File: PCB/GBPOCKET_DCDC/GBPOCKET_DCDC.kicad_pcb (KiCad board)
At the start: 2 copper layers, 23 parts, among them J1 Conn_01x03, J2 Conn_01x02, U1 MCP1623, U2 MAX868

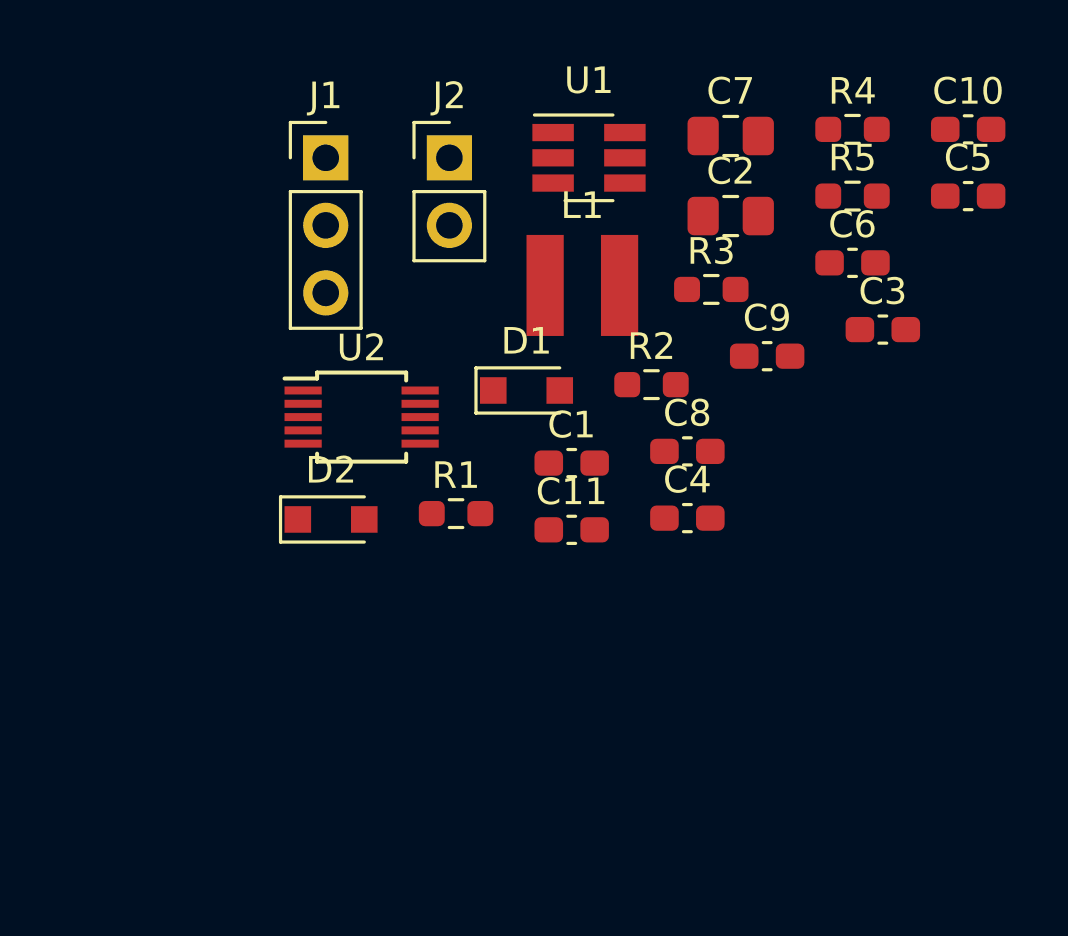
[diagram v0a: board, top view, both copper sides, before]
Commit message: Updated schematic a bit Added header for LED Finished PCB (quick'n'dirty, bit it'll do) Exported gerbers for production
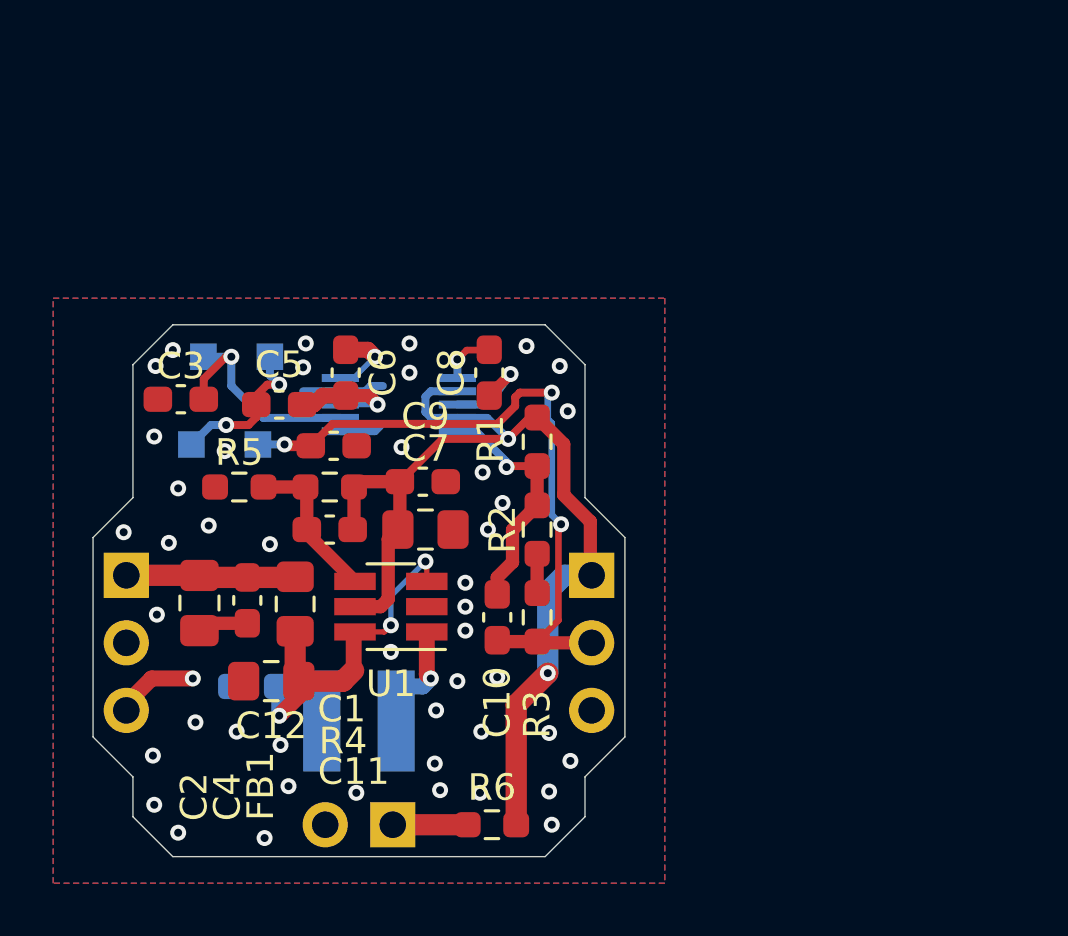
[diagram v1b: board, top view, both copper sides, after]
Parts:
- added C12: 10uF, Capacitor_SMD:C_0805_2012Metric_Pad1.18x1.45mm_HandSolder, F.Cu at (125.2, 93.4)
- added C13: 100nF, Capacitor_SMD:C_0603_1608Metric_Pad1.08x0.95mm_HandSolder, B.Cu at (124.6, 93.6)
- added FB1: Ferrite_Bead, Inductor_SMD:L_0805_2012Metric_Pad1.15x1.40mm_HandSolder, F.Cu at (126.1, 90.5)
- added J3: Conn_01x02, Connector_PinHeader_2.54mm:PinHeader_1x02_P2.54mm_Vertical, B.Cu at (129.8, 98.8)
- added MARK1: LOGO, Kicad_Library:FOX_LOGO_SILK, B.Cu at (127.5, 88.2)
- added R6: 100R, Resistor_SMD:R_0603_1608Metric_Pad0.98x0.95mm_HandSolder, F.Cu at (133.5, 98.8)
- D1, D2, J1, L1, U2: moved to B.Cu
- J2: value Conn_01x02 -> Conn_01x03; footprint Connector_PinHeader_2.54mm:PinHeader_1x02_P2.54mm_Vertical -> Connector_PinHeader_2.54mm:PinHeader_1x03_P2.54mm_Vertical; moved to B.Cu
- moved C5 27.1 mm to (125.5, 83.0)
- moved C3 26.5 mm to (121.8, 82.8), turned to 180 degrees
- moved R5 25.5 mm to (124.0, 86.1), turned to 180 degrees
- moved C10 25.5 mm to (133.7, 91.0), turned to 270 degrees
- moved C2 24.7 mm to (122.5, 90.5), turned to 270 degrees
- moved R4 23.8 mm to (127.4, 86.1), turned to 180 degrees
- moved J2 19.9 mm to (119.8, 89.4), turned to 180 degrees
- moved C6 19.5 mm to (128.0, 81.8), turned to 90 degrees
- moved C7 18.7 mm to (131.0, 87.7)
- moved J1 18.6 mm to (137.2, 89.4), turned to 180 degrees
- moved U1 18.5 mm to (129.7, 90.6), turned to 180 degrees
- moved L1 18.4 mm to (128.5, 94.9), turned to 180 degrees
- moved C4 16.8 mm to (124.3, 90.4), turned to 270 degrees
- moved R3 14.0 mm to (135.2, 91.0), turned to 270 degrees
- moved C9 13.8 mm to (130.9, 85.9)
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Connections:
- J2 pad 2: GND -> (no net)
- L1 pad 2: Net-(L1-Pad2) -> +VSW
- U1 pad 3: +BATT -> +VSW
- U1 pad 6: Net-(L1-Pad2) -> +VSW
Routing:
- net +5V: track 0.00 -> 38.9 mm, vias 0 -> 2
- net -18V: track 0.00 -> 25.7 mm, vias 0 -> 3
- net +VSW: track 0.00 -> 16.5 mm, vias 0 -> 3
- net GND: track 0.00 -> 9.72 mm, vias 0 -> 46
- net /FB_NEG: track 0.00 -> 9.14 mm, vias 0 -> 1
- net Net-(C3-Pad1): track 0.00 -> 8.89 mm, vias 0 -> 1
- net +BATT: track 0.00 -> 6.39 mm
- net Net-(C5-Pad1): track 0.00 -> 5.90 mm, vias 0 -> 2
- net /FB: track 0.00 -> 5.90 mm
- net Net-(C5-Pad2): track 0.00 -> 4.57 mm, vias 0 -> 1
- net Net-(C8-Pad1): track 0.00 -> 3.72 mm, vias 0 -> 1
- net Net-(L1-Pad1): track 0.00 -> 3.34 mm, vias 0 -> 1
- net Net-(C6-Pad2): track 0.00 -> 2.89 mm, vias 0 -> 1
- net Net-(J3-Pad1): track 0.00 -> 2.82 mm
- net Net-(C8-Pad2): track 0.00 -> 2.09 mm, vias 0 -> 1
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- added copper zone on B.Cu, net GND
- added copper zone on F.Cu, net GND
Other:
- board outline added: 20 x 20 mm
- board text added: "+5V"
- board text added: "-18V"
- board text added: "DESIGNER NOTES - Original PCB is 1mm thick - This view is from the FRONT of the Gameboy PCB (ie. where the buttons are) - Distance between PCBs is 2.5mm to 2.8mm, depending on where it is measured"
- board text added: "GND"
- board text added: "VBAT"
